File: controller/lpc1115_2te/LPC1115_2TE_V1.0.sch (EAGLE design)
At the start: 52 parts, among them IC1 LPC1115, IC2 BD9G101, Q1 BC856, Q2 BC847C, Q3 BCP52, Q4 FA-

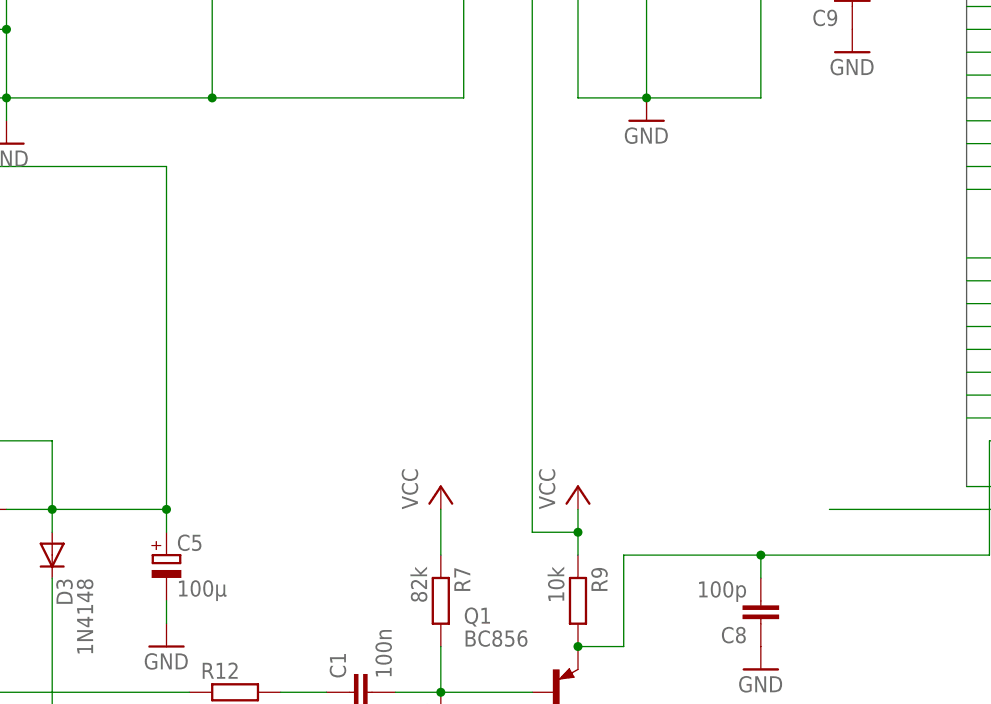
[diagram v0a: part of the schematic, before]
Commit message: BUS-ADC zugefügt
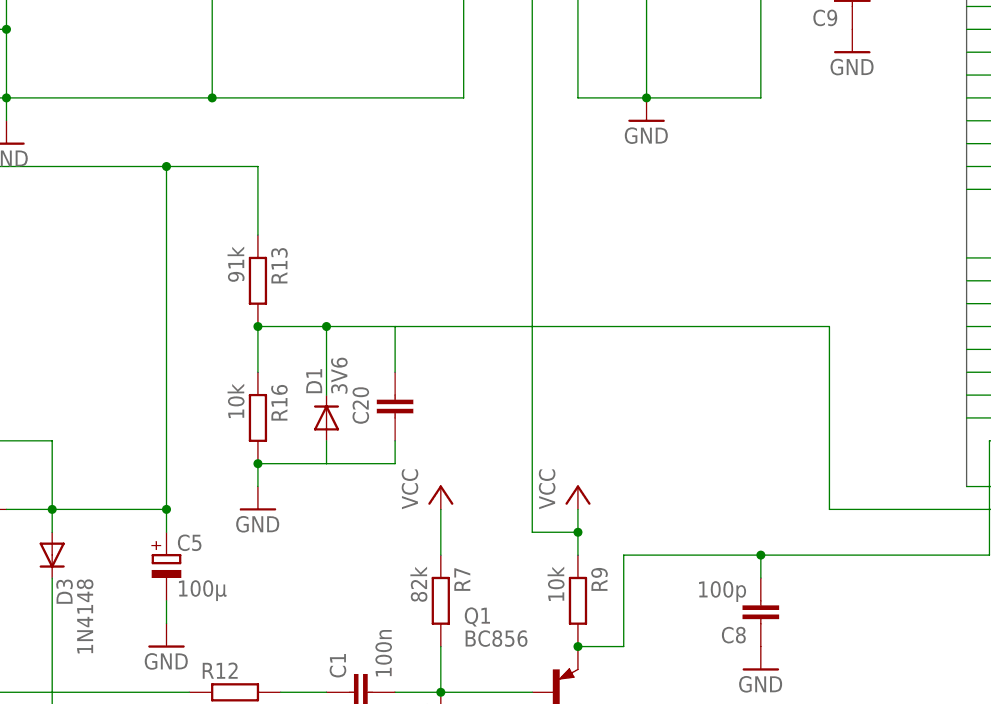
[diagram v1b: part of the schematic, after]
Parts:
- added C20: (no value), rcl:C-EUC1206
- added D1: 3V6, diode:DIODE-MINIMELF
- added R13: 91k, rcl:R-EU_R1206
- added R16: 10k, rcl:R-EU_R1206
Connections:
- net BUS_V: now also C20.2, D1.C, R13.2, R16.1
- net EIB_DC: now also R13.1
- net GND: now also C20.1, D1.A, R16.2
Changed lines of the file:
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@@
 <part name="GND25" library="supply1" deviceset="GND" device=""/>
 <part name="C6" library="rcl" deviceset="C-EU" device="C1206" value="100n"/>
+<part name="GND17" library="supply1" deviceset="GND" device=""/>
+<part name="R13" library="rcl" deviceset="R-EU_" device="R1206" value="91k"/>
+<part name="R16" library="rcl" deviceset="R-EU_" device="R1206" value="10k"/>
+<part name="D1" library="diode" deviceset="DIODE-" device="MINIMELF" value="3V6"/>
+<part name="C20" library="rcl" deviceset="C-EU" device="C1206"/>
 </parts>
 <sheets>
@@
 <instance part="GND25" gate="1" x="172.72" y="170.18"/>
 <instance part="C6" gate="G$1" x="142.24" y="180.34" rot="MR180"/>
+<instance part="GND17" gate="1" x="106.68" y="119.38"/>
+<instance part="R13" gate="G$1" x="106.68" y="144.78" rot="R270"/>
+<instance part="R16" gate="G$1" x="106.68" y="129.54" rot="R270"/>
+<instance part="D1" gate="G$1" x="114.3" y="129.54" rot="R90"/>
+<instance part="C20" gate="G$1" x="121.92" y="129.54" smashed="yes" rot="R180">
+<attribute name="NAME" x="117.221" y="133.096" size="1.778" layer="95" rot="R270"/>
+<attribute name="VALUE" x="119.761" y="128.016" size="1.778" layer="96" rot="R270"/>
+</instance>
 </instances>
 <busses>
@@
 <pinref part="C9" gate="G$1" pin="1"/>
 <pinref part="GND25" gate="1" pin="GND"/>
+</segment>
+<segment>
+<pinref part="R16" gate="G$1" pin="2"/>
+<pinref part="GND17" gate="1" pin="GND"/>
+<wire x1="106.68" y1="121.92" x2="106.68" y2="124.46" width="0.1524" layer="91"/>
+<pinref part="D1" gate="G$1" pin="A"/>
+<wire x1="106.68" y1="124.46" x2="114.3" y2="124.46" width="0.1524" layer="91"/>
+<wire x1="114.3" y1="124.46" x2="114.3" y2="127" width="0.1524" layer="91"/>
+<junction x="106.68" y="124.46"/>
+<wire x1="114.3" y1="124.46" x2="121.92" y2="124.46" width="0.1524" layer="91"/>
+<pinref part="C20" gate="G$1" pin="1"/>
+<wire x1="121.92" y1="124.46" x2="121.92" y2="127" width="0.1524" layer="91"/>
 </segment>
 </net>
@@
 <net name="EIB_DC" class="0">
 <segment>
+<wire x1="391.16" y1="139.7" x2="416.56" y2="139.7" width="0.1524" layer="91"/>
+<wire x1="416.56" y1="139.7" x2="416.56" y2="213.36" width="0.1524" layer="91"/>
+<label x="393.7" y="139.7" size="1.778" layer="95"/>
+</segment>
+<segment>
+<wire x1="106.68" y1="149.86" x2="106.68" y2="157.48" width="0.1524" layer="91"/>
+<pinref part="R13" gate="G$1" pin="1"/>
 <wire x1="96.52" y1="116.84" x2="96.52" y2="119.38" width="0.1524" layer="91"/>
 <wire x1="96.52" y1="119.38" x2="96.52" y2="157.48" width="0.1524" layer="91"/>
@@
 <wire x1="96.52" y1="157.48" x2="17.78" y2="157.48" width="0.1524" layer="91"/>
 <wire x1="17.78" y1="157.48" x2="17.78" y2="195.58" width="0.1524" layer="91"/>
-</segment>
-<segment>
-<wire x1="391.16" y1="139.7" x2="416.56" y2="139.7" width="0.1524" layer="91"/>
-<wire x1="416.56" y1="139.7" x2="416.56" y2="213.36" width="0.1524" layer="91"/>
-<label x="393.7" y="139.7" size="1.778" layer="95"/>
+<wire x1="106.68" y1="157.48" x2="96.52" y2="157.48" width="0.1524" layer="91"/>
+<junction x="96.52" y="157.48"/>
 </segment>
 </net>
@@
 </segment>
 </net>
-<net name="BUS_V" class="0">
-<segment>
-<pinref part="IC1" gate="G$1" pin="PIO1_11/AD7/CT32B1_CAP1"/>
-<wire x1="170.18" y1="119.38" x2="205.74" y2="119.38" width="0.1524" layer="91"/>
-<label x="203.2" y="119.38" size="1.778" layer="95" rot="MR0"/>
-</segment>
-</net>
 <net name="TXD" class="0">
 <segment>
@@
 </segment>
 </net>
+<net name="BUS_V" class="0">
+<segment>
+<wire x1="106.68" y1="139.7" x2="114.3" y2="139.7" width="0.1524" layer="91"/>
+<wire x1="114.3" y1="139.7" x2="121.92" y2="139.7" width="0.1524" layer="91"/>
+<wire x1="121.92" y1="139.7" x2="170.18" y2="139.7" width="0.1524" layer="91"/>
+<pinref part="R13" gate="G$1" pin="2"/>
+<pinref part="R16" gate="G$1" pin="1"/>
+<junction x="106.68" y="139.7"/>
+<pinref part="D1" gate="G$1" pin="C"/>
+<wire x1="114.3" y1="132.08" x2="114.3" y2="139.7" width="0.1524" layer="91"/>
+<junction x="114.3" y="139.7"/>
+<wire x1="106.68" y1="139.7" x2="106.68" y2="134.62" width="0.1524" layer="91"/>
+<pinref part="C20" gate="G$1" pin="2"/>
+<wire x1="121.92" y1="134.62" x2="121.92" y2="139.7" width="0.1524" layer="91"/>
+<pinref part="IC1" gate="G$1" pin="PIO1_11/AD7/CT32B1_CAP1"/>
+<wire x1="170.18" y1="119.38" x2="205.74" y2="119.38" width="0.1524" layer="91"/>
+<label x="203.2" y="119.38" size="1.778" layer="95" rot="MR0"/>
+<wire x1="170.18" y1="139.7" x2="170.18" y2="119.38" width="0.1524" layer="91"/>
+</segment>
+</net>
